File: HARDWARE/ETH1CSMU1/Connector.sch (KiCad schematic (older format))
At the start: 1 part, among them J1101 C96ABC

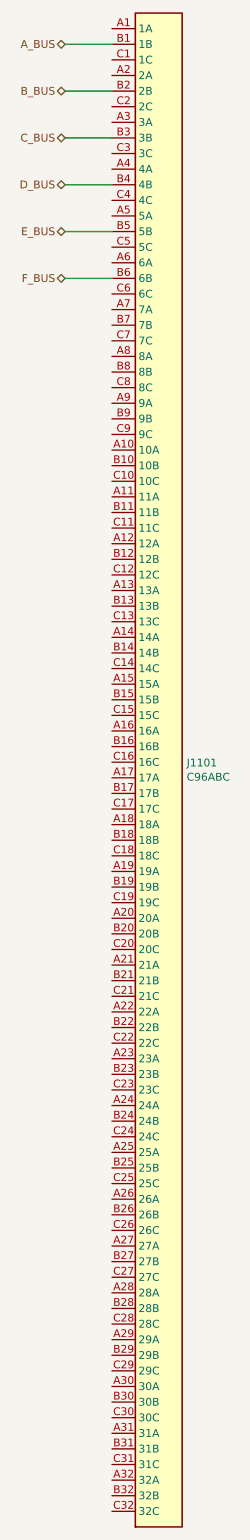
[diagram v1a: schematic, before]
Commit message: Footprint selection
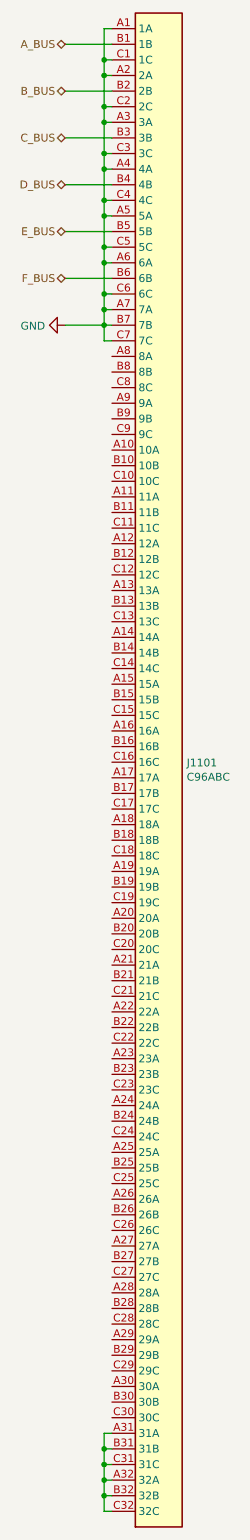
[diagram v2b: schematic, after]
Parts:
- J1101: footprint (none) -> Connectors_IEC_DIN:Socket_DIN41612-CaseC1-full-Male-96Pin-3rows
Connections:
- net GND: now reaches J1101.A1 (1A)
- net GND: now also J1101.A2 (2A), J1101.A3 (3A), J1101.A4 (4A), J1101.A5 (5A), J1101.A6 (6A), J1101.A7 (7A), J1101.B7 (7B), J1101.C1 (1C), J1101.C2 (2C), J1101.C3 (3C), J1101.C4 (4C), J1101.C5 (5C), J1101.C6 (6C), J1101.C7 (7C)
- net at J1101.A31 (31A): now also J1101.A32 (32A), J1101.B31 (31B), J1101.B32 (32B), J1101.C31 (31C), J1101.C32 (32C)
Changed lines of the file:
@@
 F 0 "J1101" H 8429 5846 50  0000 L CNN
 F 1 "C96ABC" H 8429 5755 50  0000 L CNN
-F 2 "" H 8250 5800 50  0001 C CNN
+F 2 "Connectors_IEC_DIN:Socket_DIN41612-CaseC1-full-Male-96Pin-3rows" H 8250 5800 50  0001 C CNN
 F 3 " ~" H 8250 5800 50  0001 C CNN
 	1    8250 5750
@@
 Text HLabel 7650 2550 0    50   BiDi ~ 0
 F_BUS
+Wire Wire Line
+	7950 950  7900 950
+Wire Wire Line
+	7900 950  7900 1150
+Wire Wire Line
+	7900 2650 7950 2650
+Wire Wire Line
+	7950 2450 7900 2450
+Connection ~ 7900 2450
+Wire Wire Line
+	7900 2450 7900 2650
+Wire Wire Line
+	7950 2150 7900 2150
+Connection ~ 7900 2150
+Wire Wire Line
+	7900 2150 7900 2350
+Wire Wire Line
+	7950 2350 7900 2350
+Connection ~ 7900 2350
+Wire Wire Line
+	7900 2350 7900 2450
+Wire Wire Line
+	7950 2050 7900 2050
+Connection ~ 7900 2050
+Wire Wire Line
+	7900 2050 7900 2150
+Wire Wire Line
+	7950 1850 7900 1850
+Connection ~ 7900 1850
+Wire Wire Line
+	7900 1850 7900 2050
+Wire Wire Line
+	7950 1750 7900 1750
+Connection ~ 7900 1750
+Wire Wire Line
+	7900 1750 7900 1850
+Wire Wire Line
+	7950 1550 7900 1550
+Connection ~ 7900 1550
+Wire Wire Line
+	7900 1550 7900 1750
+Wire Wire Line
+	7950 1450 7900 1450
+Connection ~ 7900 1450
+Wire Wire Line
+	7900 1450 7900 1550
+Wire Wire Line
+	7950 1250 7900 1250
+Connection ~ 7900 1250
+Wire Wire Line
+	7900 1250 7900 1450
+Wire Wire Line
+	7950 1150 7900 1150
+Connection ~ 7900 1150
+Wire Wire Line
+	7900 1150 7900 1250
+Wire Wire Line
+	7950 10250 7900 10250
+Wire Wire Line
+	7900 10250 7900 10350
+Wire Wire Line
+	7900 10450 7950 10450
+Wire Wire Line
+	7950 10350 7900 10350
+Connection ~ 7900 10350
+Wire Wire Line
+	7900 10350 7900 10450
+Wire Wire Line
+	7950 10150 7900 10150
+Wire Wire Line
+	7900 10150 7900 10050
+Wire Wire Line
+	7900 9950 7950 9950
+Wire Wire Line
+	7950 10050 7900 10050
+Connection ~ 7900 10050
+Wire Wire Line
+	7900 10050 7900 9950
+Wire Wire Line
+	7900 10150 7900 10250
+Connection ~ 7900 10150
+Connection ~ 7900 10250
+$Comp
+L power:GND #PWR0131
+U 1 1 5C06D98A
+P 7650 2850
+F 0 "#PWR0131" H 7650 2600 50  0001 C CNN
+F 1 "GND" V 7655 2722 50  0000 R CNN
+F 2 "" H 7650 2850 50  0001 C CNN
+F 3 "" H 7650 2850 50  0001 C CNN
+	1    7650 2850
+	0    1    1    0
+$EndComp
+Wire Wire Line
+	7950 2950 7900 2950
+Wire Wire Line
+	7900 2950 7900 2850
+Connection ~ 7900 2650
+Wire Wire Line
+	7950 2750 7900 2750
+Connection ~ 7900 2750
+Wire Wire Line
+	7900 2750 7900 2650
+Wire Wire Line
+	7950 2850 7900 2850
+Connection ~ 7900 2850
+Wire Wire Line
+	7900 2850 7900 2750
+Wire Wire Line
+	7650 2850 7900 2850
 $EndSCHEMATC

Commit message: Schematic development
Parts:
- added FB1001: MPZ2012S221A, symbol Device:Ferrite_Bead_Small
- renumbered J1101 to J1001
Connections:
- net GND: now also FB1001.2; no longer J1001.A1 (1A), J1001.A2 (2A), J1001.A3 (3A), J1001.A4 (4A), J1001.A5 (5A), J1001.A6 (6A), J1001.A7 (7A), J1001.B7 (7B), J1001.C1 (1C), J1001.C2 (2C), J1001.C3 (3C), J1001.C4 (4C), J1001.C5 (5C), J1001.C6 (6C), J1001.C7 (7C)
- net GNDPWR: now reaches J1001.A27 (27A)
- net GNDPWR: now also J1001.A28 (28A), J1001.B27 (27B), J1001.B28 (28B), J1001.C27 (27C), J1001.C28 (28C)
- net +24V: now reaches J1001.A31 (31A), J1001.A32 (32A), J1001.B31 (31B), J1001.B32 (32B), J1001.C31 (31C), J1001.C32 (32C)
- new net: FB1001.1, J1001.A1 (1A), J1001.A2 (2A), J1001.A3 (3A), J1001.A4 (4A), J1001.A5 (5A), J1001.A6 (6A), J1001.A7 (7A), J1001.B7 (7B), J1001.C1 (1C), J1001.C2 (2C), J1001.C3 (3C), J1001.C4 (4C), J1001.C5 (5C), J1001.C6 (6C), J1001.C7 (7C)
- no-connect marks 0 -> 6
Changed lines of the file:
@@
 $Descr A3 16535 11693
 encoding utf-8
-Sheet 11 14
+Sheet 10 15
 Title ""
 Date ""
@@
 $EndDescr
 $Comp
-L Connector:C96ABC J1101
+L Connector:C96ABC J1001
 U 1 1 5BE3062A
 P 8250 5750
-F 0 "J1101" H 8429 5846 50  0000 L CNN
+F 0 "J1001" H 8429 5846 50  0000 L CNN
 F 1 "C96ABC" H 8429 5755 50  0000 L CNN
 F 2 "Connectors_IEC_DIN:Socket_DIN41612-CaseC1-full-Male-96Pin-3rows" H 8250 5800 50  0001 C CNN
@@
 Connection ~ 7900 10250
 $Comp
-L power:GND #PWR0131
+L power:GND #PWR01001
 U 1 1 5C06D98A
-P 7650 2850
-F 0 "#PWR0131" H 7650 2600 50  0001 C CNN
-F 1 "GND" V 7655 2722 50  0000 R CNN
-F 2 "" H 7650 2850 50  0001 C CNN
-F 3 "" H 7650 2850 50  0001 C CNN
-	1    7650 2850
+P 7100 2950
+F 0 "#PWR01001" H 7100 2700 50  0001 C CNN
+F 1 "GND" V 7105 2822 50  0000 R CNN
+F 2 "" H 7100 2950 50  0001 C CNN
+F 3 "" H 7100 2950 50  0001 C CNN
+	1    7100 2950
 	0    1    1    0
 $EndComp
@@
 	7900 2850 7900 2750
 Wire Wire Line
-	7650 2850 7900 2850
+	7100 2950 7350 2950
+$Comp
+L Device:Ferrite_Bead_Small FB1001
+U 1 1 5C0DCC9D
+P 7450 2950
+F 0 "FB1001" V 7213 2950 50  0000 C CNN
+F 1 "MPZ2012S221A" V 7304 2950 50  0000 C CNN
+F 2 "" V 7380 2950 50  0001 C CNN
+F 3 "~" H 7450 2950 50  0001 C CNN
+	1    7450 2950
+	0    1    1    0
+$EndComp
+Wire Wire Line
+	7550 2950 7900 2950
+Connection ~ 7900 2950
+NoConn ~ 7950 9850
+NoConn ~ 7950 9750
+NoConn ~ 7950 9650
+NoConn ~ 7950 9550
+NoConn ~ 7950 9450
+NoConn ~ 7950 9350
+Wire Wire Line
+	7950 9050 7900 9050
+Wire Wire Line
+	7900 9050 7900 9150
+Wire Wire Line
+	7900 9250 7950 9250
+Wire Wire Line
+	7950 9150 7900 9150
+Connection ~ 7900 9150
+Wire Wire Line
+	7900 9150 7900 9250
+Wire Wire Line
+	7950 8950 7900 8950
+Wire Wire Line
+	7900 8950 7900 8850
+Wire Wire Line
+	7900 8750 7950 8750
+Wire Wire Line
+	7950 8850 7900 8850
+Connection ~ 7900 8850
+Wire Wire Line
+	7900 8850 7900 8750
+Wire Wire Line
+	7900 8950 7900 9050
+Connection ~ 7900 8950
+Connection ~ 7900 9050
+$Comp
+L power:+24V #PWR0101
+U 1 1 5C11EB76
+P 7850 10450
+F 0 "#PWR0101" H 7850 10300 50  0001 C CNN
+F 1 "+24V" V 7865 10578 50  0000 L CNN
+F 2 "" H 7850 10450 50  0001 C CNN
+F 3 "" H 7850 10450 50  0001 C CNN
+	1    7850 10450
+	0    -1   -1   0
+$EndComp
+Wire Wire Line
+	7850 10450 7900 10450
+Connection ~ 7900 10450
+$Comp
+L power:GNDPWR #PWR0102
+U 1 1 5C122004
+P 7850 9250
+F 0 "#PWR0102" H 7850 9050 50  0001 C CNN
+F 1 "GNDPWR" V 7854 9141 50  0000 R CNN
+F 2 "" H 7850 9200 50  0001 C CNN
+F 3 "" H 7850 9200 50  0001 C CNN
+	1    7850 9250
+	0    1    1    0
+$EndComp
+Wire Wire Line
+	7850 9250 7900 9250
+Connection ~ 7900 9250
 $EndSCHEMATC

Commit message: check in
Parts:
- FB1001: footprint (none) -> SMD:R_0805_Symbol1
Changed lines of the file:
@@
 F 0 "FB1001" V 7213 2950 50  0000 C CNN
 F 1 "MPZ2012S221A" V 7304 2950 50  0000 C CNN
-F 2 "" V 7380 2950 50  0001 C CNN
+F 2 "SMD:R_0805_Symbol1" V 7380 2950 50  0001 C CNN
 F 3 "~" H 7450 2950 50  0001 C CNN
 	1    7450 2950
@@
 	7850 9250 7900 9250
 Connection ~ 7900 9250
+Text HLabel 5650 2250 0    50   BiDi ~ 0
+CODE_0
+Text HLabel 5650 2350 0    50   BiDi ~ 0
+CODE_1
+Text HLabel 5650 2450 0    50   BiDi ~ 0
+CODE_2
+Text HLabel 5650 2550 0    50   BiDi ~ 0
+CODE_3
+Text HLabel 5650 2650 0    50   UnSpc ~ 0
+CODE_3V3
 $EndSCHEMATC
